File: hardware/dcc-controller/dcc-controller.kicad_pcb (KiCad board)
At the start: 2 copper layers, 100 x 62 mm, 45 parts, among them IC1 DRV8231DSGR, J1 Screw_Terminal_01x04, SW1 SW_DIP_x07, SW2 E_STOP, SW3 PROG_BTN, SW4 PROG_MODE, SW5 SW_DIP_x07, SW6 SW_PWR, U1 STM32F103C6Tx, U2 4001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

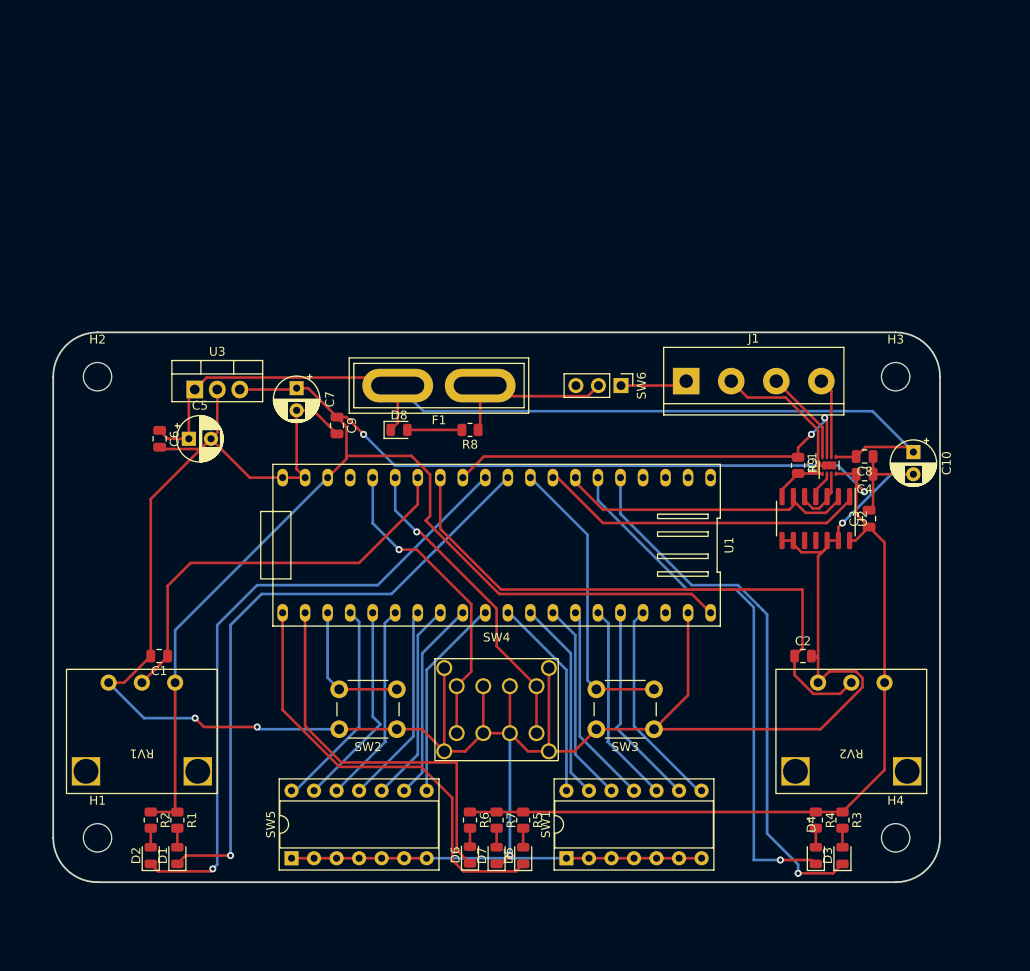
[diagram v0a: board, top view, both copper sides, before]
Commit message: Update schematic for display
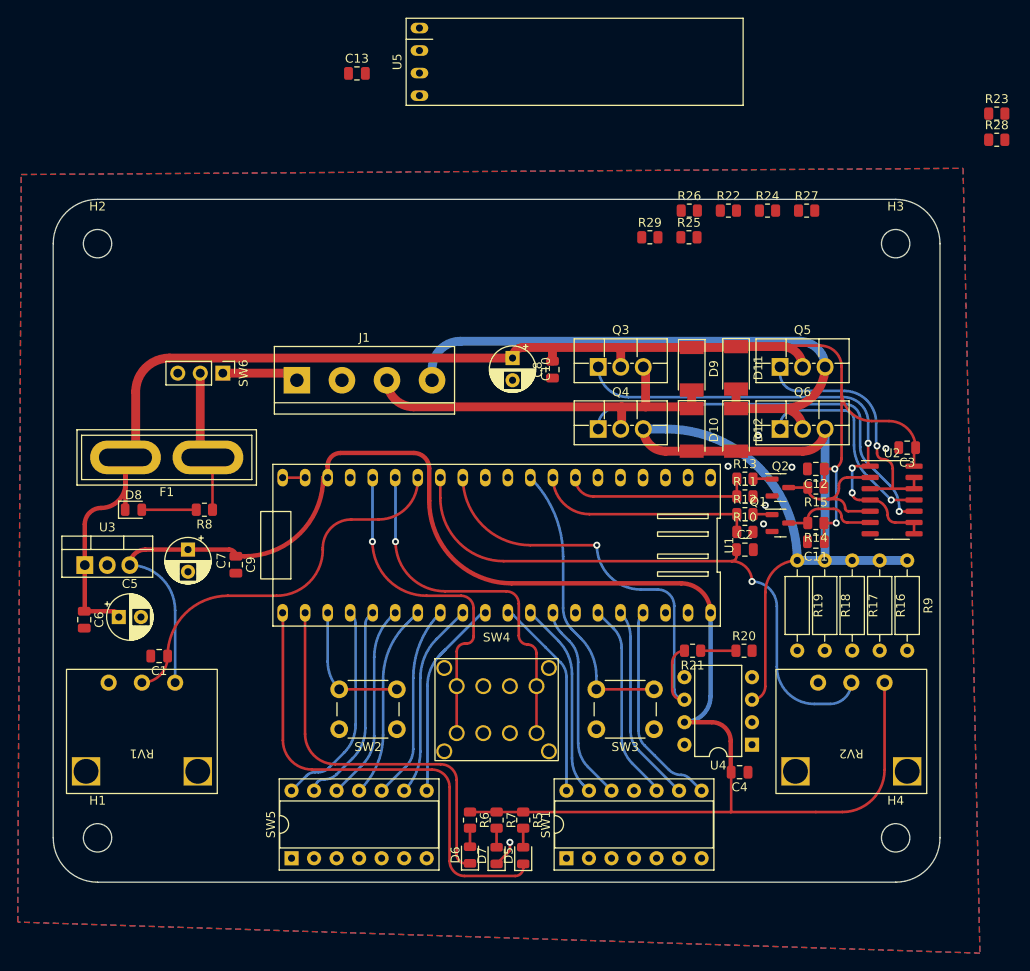
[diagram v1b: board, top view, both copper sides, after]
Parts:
- removed D1: 1F, LED_SMD:LED_0805_2012Metric
- removed D2: 1R, LED_SMD:LED_0805_2012Metric
- removed D3: 2F, LED_SMD:LED_0805_2012Metric
- removed D4: 2R, LED_SMD:LED_0805_2012Metric
- removed IC1: DRV8231DSGR, Package_SON:WSON-8-1EP_2x2mm_P0.5mm_EP0.9x1.6mm
- removed R1, R2, R3, R4: 330, Resistor_SMD:R_0805_2012Metric
- added C11: 10n, Capacitor_SMD:C_0805_2012Metric, F.Cu at (188.0, 93.6)
- added C12: 10n, Capacitor_SMD:C_0805_2012Metric, F.Cu at (188.0, 85.4)
- added C13: 100n, Capacitor_SMD:C_0805_2012Metric, F.Cu at (136.2, 40.8)
- added D10: D, Diode_SMD:D_MELF, F.Cu at (174.0, 81.0)
- added D11: D, Diode_SMD:D_MELF, F.Cu at (179.0, 74.0)
- added D12: D, Diode_SMD:D_MELF, F.Cu at (179.0, 81.0)
- added D9: D, Diode_SMD:D_MELF, F.Cu at (174.0, 74.1)
- added Q1: CMPDM7003, Package_TO_SOT_SMD:SOT-23, F.Cu at (184.0, 91.5)
- added Q2: CMPDM7003, Package_TO_SOT_SMD:SOT-23, F.Cu at (184.0, 87.5)
- added Q3: IRF520PBF, Package_TO_SOT_THT:TO-220F-3_Vertical, F.Cu at (163.5, 73.9)
- added Q4: IRF520PBF, Package_TO_SOT_THT:TO-220F-3_Vertical, F.Cu at (163.5, 80.9)
- added Q5: IRF520PBF, Package_TO_SOT_THT:TO-220F-3_Vertical, F.Cu at (184.0, 73.9)
- added Q6: IRF520PBF, Package_TO_SOT_THT:TO-220F-3_Vertical, F.Cu at (184.0, 80.9)
- added R10: 100k, Resistor_SMD:R_0805_2012Metric, F.Cu at (180.0, 92.5)
- added R11: 100k, Resistor_SMD:R_0805_2012Metric, F.Cu at (180.0, 88.5)
- added R12: 100, Resistor_SMD:R_0805_2012Metric, F.Cu at (180.0, 90.5)
- added R13: 100, Resistor_SMD:R_0805_2012Metric, F.Cu at (180.0, 86.5)
- added R14: 10k, Resistor_SMD:R_0805_2012Metric, F.Cu at (188.0, 91.5)
- added R15: 10k, Resistor_SMD:R_0805_2012Metric, F.Cu at (188.0, 87.5)
- added R16: 1R 1W, Resistor_THT:R_Axial_DIN0207_L6.3mm_D2.5mm_P10.16mm_Horizontal, F.Cu at (195.2, 95.7)
- added R17: 1R 1W, Resistor_THT:R_Axial_DIN0207_L6.3mm_D2.5mm_P10.16mm_Horizontal, F.Cu at (192.1, 95.7)
- added R18: 1R 1W, Resistor_THT:R_Axial_DIN0207_L6.3mm_D2.5mm_P10.16mm_Horizontal, F.Cu at (189.0, 95.7)
- added R19: 1R 1W, Resistor_THT:R_Axial_DIN0207_L6.3mm_D2.5mm_P10.16mm_Horizontal, F.Cu at (185.9, 95.7)
- added R20: 25k, Resistor_SMD:R_0805_2012Metric, F.Cu at (179.9, 105.9)
- added R21: 100k, Resistor_SMD:R_0805_2012Metric, F.Cu at (174.1, 105.9)
- added R22: 100k, Resistor_SMD:R_0805_2012Metric, F.Cu at (178.1, 56.3)
- added R23: 100, Resistor_SMD:R_0805_2012Metric, F.Cu at (208.4, 45.3)
- added R24: 100, Resistor_SMD:R_0805_2012Metric, F.Cu at (182.6, 56.3)
- added R25: 100k, Resistor_SMD:R_0805_2012Metric, F.Cu at (173.7, 59.3)
- added R26: 100, Resistor_SMD:R_0805_2012Metric, F.Cu at (173.7, 56.3)
- added R27: 100k, Resistor_SMD:R_0805_2012Metric, F.Cu at (187.0, 56.3)
- added R28: 100, Resistor_SMD:R_0805_2012Metric, F.Cu at (208.4, 48.3)
- added R29: 100k, Resistor_SMD:R_0805_2012Metric, F.Cu at (169.3, 59.3)
- added U4: LM741, Package_DIP:DIP-8_W7.62mm, F.Cu at (180.8, 116.5)
- added U5: ssd1306-display, ssd1306-display:ssd1306-display, F.Cu at (153.2, 39.5)
- R9: value 1k5 -> 1R 1W; footprint Resistor_SMD:R_0805_2012Metric -> Resistor_THT:R_Axial_DIN0207_L6.3mm_D2.5mm_P10.16mm_Horizontal
- moved C10 46.4 mm to (153.8, 72.9)
- moved SW6 44.9 mm to (121.1, 74.6)
- moved J1 43.9 mm to (129.5, 75.4)
- moved C8 36.5 mm to (158.3, 74.2), turned to 90 degrees
- moved C4 36.4 mm to (179.4, 119.6)
- moved F1 31.8 mm to (119.5, 84.1)
- moved D8 31.3 mm to (111.0, 90.0)
- moved R8 31.3 mm to (119.0, 90.0)
- moved U3 23.4 mm to (105.6, 96.2)
- moved C6 22.1 mm to (105.5, 102.4)
- moved C7 21.9 mm to (117.2, 94.5)
- moved C5 21.6 mm to (109.4, 102.1)
- moved C9 19.4 mm to (122.6, 96.2)
- moved R9 16.3 mm to (198.3, 95.7)
- moved H2 15.0 mm to (107.0, 60.0)
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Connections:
- C3 pad 1: +3V3 -> +12V
- R9 pad 1: CURRENT -> /SHUNT
- SW1 pad 10: Net-(SW1-Pad10) -> Net-(U1-Pad11)
- SW1 pad 11: Net-(SW1-Pad11) -> Net-(U1-Pad10)
- U1 pad 10: LED_1F -> Net-(U1-Pad10)
- U1 pad 11: LED_1R -> Net-(U1-Pad11)
- U1 pad 34: Net-(SW1-Pad11) -> SCL
- U1 pad 35: Net-(SW1-Pad10) -> SDA
- U1 pad 5: LED_2F -> unconnected-(U1-Pad5)
- U1 pad 6: LED_2R -> unconnected-(U1-Pad6)
- U2 pad 1: OUT_DIR -> IN_A
- U2 pad 10: unconnected-(U2-Pad10) -> Net-(U2-Pad10)
- U2 pad 11: unconnected-(U2-Pad11) -> Net-(U2-Pad11)
- U2 pad 12: GND -> IN_B
- U2 pad 13: GND -> IN_B
- U2 pad 14: +3V3 -> +12V
- U2 pad 2: OUT_EN -> /OUT_EN_SHIFT
- U2 pad 3: /IN_1 -> IN_B
- U2 pad 4: /IN_2 -> IN_A
- U2 pad 5: /IN_1 -> /OUT_EN_SHIFT
- U2 pad 6: OUT_EN -> /OUT_DIR_SHIFT
- U2 pad 8: GND -> IN_A
- U2 pad 9: GND -> IN_A
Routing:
- net GND: track 349.5 -> 5.60 mm, vias 4 -> 6
- net /SHUNT: track 0.00 -> 94.0 mm
- net +3V3: track 274.5 -> 188.3 mm, vias 2 -> 0
- net LED_1R: track 72.3 -> 0.00 mm, vias 1 -> 0
- net LED_1F: track 70.5 -> 0.00 mm, vias 1 -> 0
- net LED_2F: track 61.4 -> 0.00 mm, vias 1 -> 0
- net LED_2R: track 60.8 -> 0.00 mm, vias 1 -> 0
- net +12V: track 109.4 -> 167.7 mm, vias 0 -> 2
- net TRACK_B: track 9.02 -> 67.0 mm
- net IN_A: track 0.00 -> 53.8 mm, vias 0 -> 3
- net Net-(U2-Pad10): track 0.00 -> 45.6 mm, vias 0 -> 1
- net TRACK_A: track 10.7 -> 45.3 mm
- net IN_B: track 0.00 -> 29.2 mm, vias 0 -> 1
- net Net-(U2-Pad11): track 0.00 -> 23.3 mm, vias 0 -> 1
- net Net-(SW1-Pad10): track 22.9 -> 0.00 mm
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- added copper zone on B.Cu, net GND
- added copper zone on F.Cu, net GND
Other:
- board size 100 x 62 mm -> 100 x 77 mm

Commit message: Do layout and routing for new display version
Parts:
- added D1: CHAN_A, LED_SMD:LED_0805_2012Metric, F.Cu at (115.3, 129.8)
- added D2: CHAN_B, LED_SMD:LED_0805_2012Metric, F.Cu at (188.7, 129.8)
- added R1: 330, Resistor_SMD:R_0805_2012Metric, F.Cu at (115.3, 127.6)
- added R2: 330, Resistor_SMD:R_0805_2012Metric, F.Cu at (188.7, 127.6)
- added TP10: TestPoint, TestPoint:TestPoint_THTPad_D2.0mm_Drill1.0mm, F.Cu at (195.9, 98.8)
- added TP11: TestPoint, TestPoint:TestPoint_THTPad_D2.0mm_Drill1.0mm, F.Cu at (105.4, 76.3)
- added TP12: TestPoint, TestPoint:TestPoint_THTPad_D2.0mm_Drill1.0mm, F.Cu at (150.1, 67.3)
- added TP13: TestPoint, TestPoint:TestPoint_THTPad_D2.0mm_Drill1.0mm, F.Cu at (108.1, 97.0)
- added TP14: TestPoint, TestPoint:TestPoint_THTPad_D2.0mm_Drill1.0mm, F.Cu at (115.4, 97.0)
- added TP15: TestPoint, TestPoint:TestPoint_THTPad_D2.0mm_Drill1.0mm, F.Cu at (199.5, 102.5)
- added TP3: TestPoint, TestPoint:TestPoint_THTPad_D2.0mm_Drill1.0mm, F.Cu at (180.3, 85.6)
- added TP4: TestPoint, TestPoint:TestPoint_THTPad_D2.0mm_Drill1.0mm, F.Cu at (180.4, 98.8)
- added TP5: TestPoint, TestPoint:TestPoint_THTPad_D2.0mm_Drill1.0mm, F.Cu at (180.2, 102.6)
- added TP6: TestPoint, TestPoint:TestPoint_THTPad_D2.0mm_Drill1.0mm, F.Cu at (196.0, 105.5)
- added TP7: TestPoint, TestPoint:TestPoint_THTPad_D2.0mm_Drill1.0mm, F.Cu at (108.1, 105.5)
- added TP8: TestPoint, TestPoint:TestPoint_THTPad_D2.0mm_Drill1.0mm, F.Cu at (199.5, 98.8)
- added TP9: TestPoint, TestPoint:TestPoint_THTPad_D2.0mm_Drill1.0mm, F.Cu at (184.2, 98.9)
- F1: footprint Fuse:Fuse_Blade_ATO_directSolder -> automotive-fuse-mount:automotive-fuse-mount
- RV1, RV2: footprint potentiometer:potentiometer vertical -> Potentiometer_THT:Potentiometer_Bourns_PTV09A-1_Single_Vertical
- SW6: footprint Connector_PinHeader_2.54mm:PinHeader_1x03_P2.54mm_Vertical -> spdt-slide-switch:spdt-slide-switch
- moved C13 61.4 mm to (130.6, 101.9), turned to -90 degrees
- moved U5 60.3 mm to (144.3, 99.1)
- moved R23 41.2 mm to (179.3, 74.5), turned to 90 degrees
- moved R28 36.2 mm to (183.5, 74.5), turned to -90 degrees
- moved R9 30.1 mm to (189.3, 67.0), turned to 0 degrees
- moved R16 26.3 mm to (189.3, 70.1), turned to 0 degrees
- moved R29 26.0 mm to (183.5, 81.0), turned to -90 degrees
- moved R27 24.8 mm to (185.6, 81.0), turned to 90 degrees
- moved R22 24.8 mm to (179.3, 81.0), turned to -90 degrees
- moved R25 23.0 mm to (181.4, 81.0), turned to -90 degrees
- moved R17 22.7 mm to (189.3, 73.2), turned to 0 degrees
- moved U4 22.2 mm to (173.6, 95.5), turned to -90 degrees
- moved R26 21.8 mm to (185.6, 74.5), turned to -90 degrees
- moved R18 19.4 mm to (189.3, 76.3), turned to 0 degrees
- moved R24 18.3 mm to (181.4, 74.5), turned to 90 degrees
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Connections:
- Q4 pad 1: GND -> /A_INV
- R23 pad 2: GND -> /A_INV
- SW1 pad 10: Net-(U1-Pad11) -> Net-(SW1-Pad10)
- SW1 pad 11: Net-(U1-Pad10) -> Net-(SW1-Pad11)
- SW6 pad 1: 12V_IN -> Net-(F1-Pad1)
- SW6 pad 2: Net-(F1-Pad1) -> 12V_IN
- SW6 pad 3: (no net) -> unconnected-(SW6-Pad3)
- U1 pad 10: Net-(U1-Pad10) -> Net-(SW1-Pad10)
- U1 pad 11: Net-(U1-Pad11) -> Net-(SW1-Pad11)
- U1 pad 5: unconnected-(U1-Pad5) -> CHAN_B
- U1 pad 6: unconnected-(U1-Pad6) -> CHAN_A
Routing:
- net CHAN_A: track 0.00 -> 114.8 mm, vias 0 -> 1
- net +3V3: track 188.3 -> 269.0 mm, vias 0 -> 1
- net CHAN_B: track 0.00 -> 76.4 mm, vias 0 -> 1
- net GND: track 5.60 -> 65.7 mm, vias 6 -> 5
- net Net-(SW1-Pad10): track 0.00 -> 59.6 mm
- net Net-(SW1-Pad11): track 0.00 -> 58.7 mm
- net POT_B: track 67.0 -> 104.2 mm, vias 1 -> 0
- net SCL: track 0.00 -> 35.6 mm
- net LED_PROG: track 54.5 -> 86.9 mm
- net LED_ALARM: track 44.0 -> 76.2 mm
- net PROG_BTN: track 32.4 -> 61.7 mm
- net Net-(Q3-Pad1): track 0.00 -> 29.0 mm, vias 0 -> 1
- net CURRENT: track 49.8 -> 78.5 mm, vias 1 -> 0
- net /A_INV: track 0.00 -> 26.5 mm, vias 0 -> 1
- net POT_A: track 43.7 -> 68.8 mm
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- added copper zone on F.Cu, net +12V
- added copper zone on F.Cu, net Net-(F1-Pad1)

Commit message: Tidy up routing
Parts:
- moved TP6 3.00 mm to (196.0, 102.5)
- moved TP5 0.22 mm to (180.4, 102.5)
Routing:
- net CHAN_A: track 114.8 -> 122.5 mm
- net +3V3: track 269.0 -> 276.6 mm
- net OUT_EN: track 34.8 -> 42.1 mm
- net PROG_MODE_2: track 50.4 -> 55.7 mm
- net PROG_MODE_1: track 49.9 -> 55.2 mm
- net OUT_DIR: track 40.9 -> 45.8 mm
- net CHAN_B: track 76.4 -> 80.4 mm
- net Net-(R22-Pad1): track 38.0 -> 41.4 mm
- net +12V: track 182.7 -> 185.9 mm
- net LED_ALARM: track 76.2 -> 79.3 mm
- net LED_PROG: track 86.9 -> 89.6 mm
- net POT_A: track 68.8 -> 71.3 mm
- net POT_B: track 104.2 -> 106.7 mm
- net IN_A: track 37.8 -> 39.9 mm
- net SCL: track 35.6 -> 37.7 mm
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
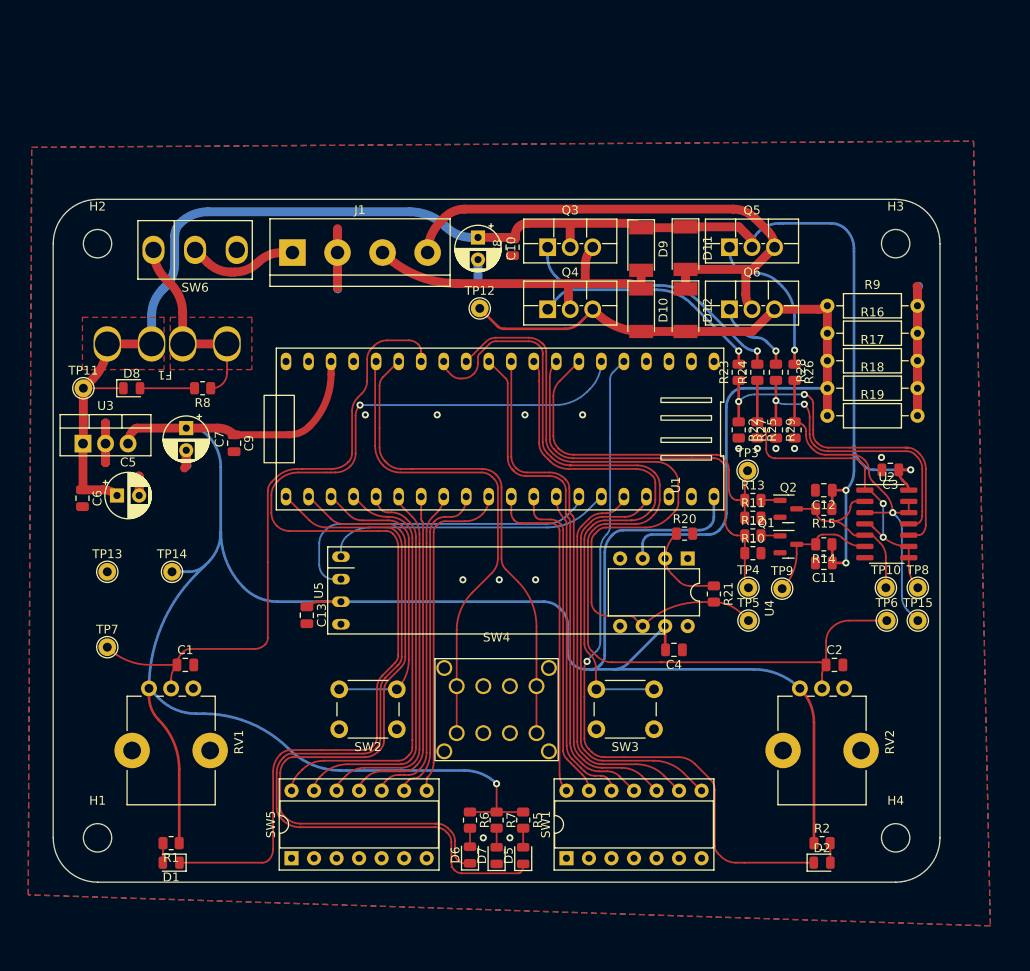
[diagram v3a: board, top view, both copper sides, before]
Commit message: Tidy up silkscreen
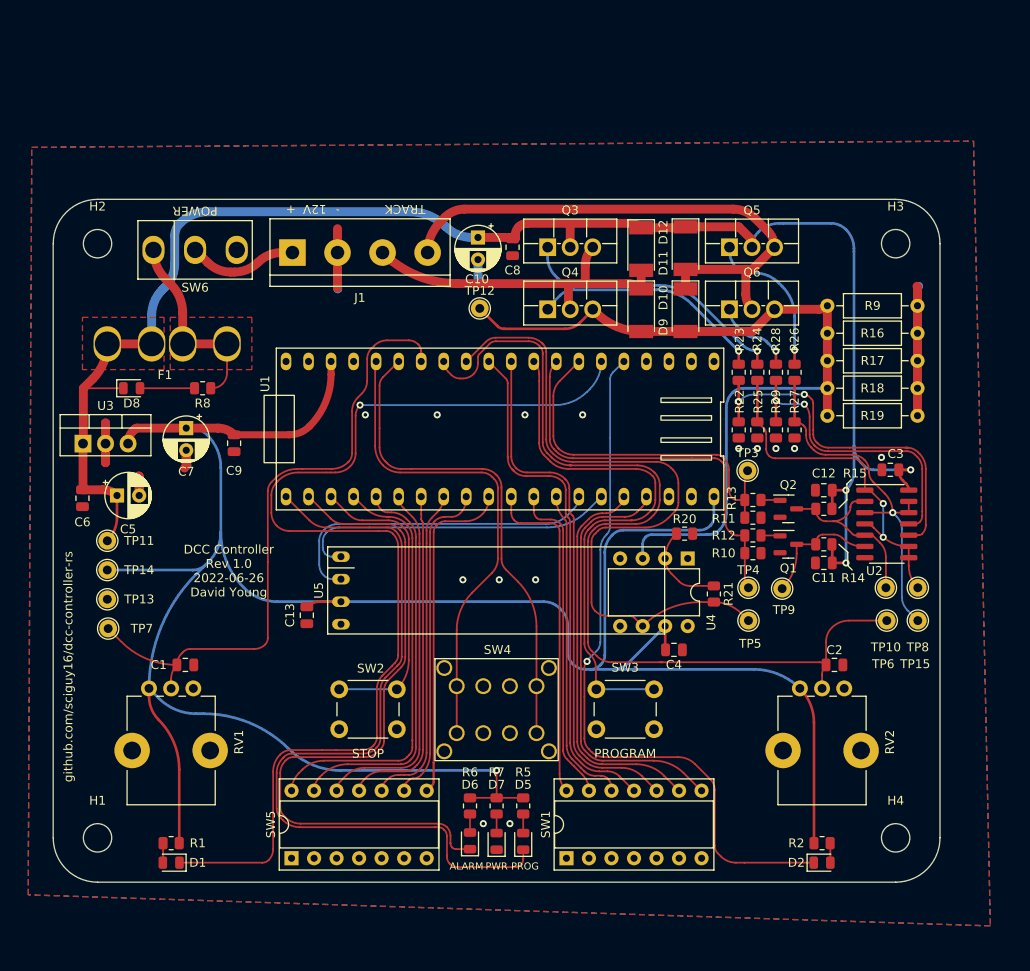
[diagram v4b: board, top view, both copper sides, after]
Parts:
- moved TP11 17.4 mm to (108.1, 93.5)
- moved TP14 7.30 mm to (108.1, 96.8)
- moved TP13 3.10 mm to (108.1, 100.1)
- moved TP7 2.10 mm to (108.2, 103.4)
- moved D5 1.60 mm to (155.0, 127.4)
- moved D6 1.60 mm to (149.0, 127.3)
- moved D7 1.60 mm to (152.0, 127.4)
- moved R5 1.60 mm to (155.0, 123.4)
- moved R6 1.60 mm to (149.0, 123.4)
- moved R7 1.60 mm to (152.0, 123.4)
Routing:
- net +3V3: track 276.6 -> 283.5 mm
- net +12V: track 185.9 -> 191.3 mm
- net SDA: track 32.6 -> 36.7 mm
- net LED_ALARM: track 79.3 -> 78.3 mm
- net POT_A: track 71.3 -> 72.0 mm
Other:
- board text added: "+"
- board text added: "-"
- board text added: "12V"
- board text added: "ALARM"
- board text added: "DCC Controller Rev 1.0 2022-06-26 David Young"
- board text added: "POWER"
- board text added: "PROG"
- board text added: "PROGRAM"
- board text added: "PWR"
- board text added: "STOP"
- board text added: "TRACK"
- board text added: "github.com/sciguy16/dcc-controller-rs"

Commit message: Add gerbers and printouts
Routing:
- net GND: track 65.7 -> 62.9 mm, vias 14 -> 16
- net PROG_BTN: track 61.6 -> 60.8 mm
- net OUT_EN: track 42.1 -> 41.5 mm
- net Net-(R28-Pad2): track 33.7 -> 33.2 mm
